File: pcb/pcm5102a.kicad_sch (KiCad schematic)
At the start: 11 parts, among them J11 PCM5102A Breakout, J12 Conn_01x03_Pin

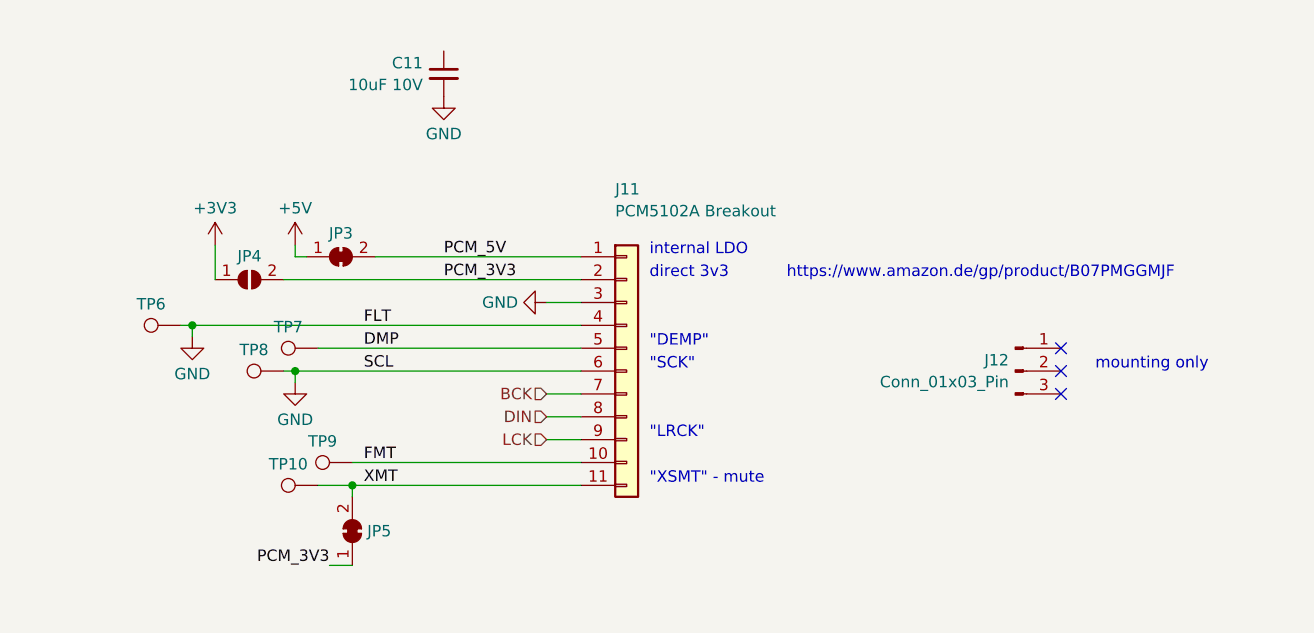
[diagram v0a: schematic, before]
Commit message: work on PCB: line out + power done ; removed amplifier from board
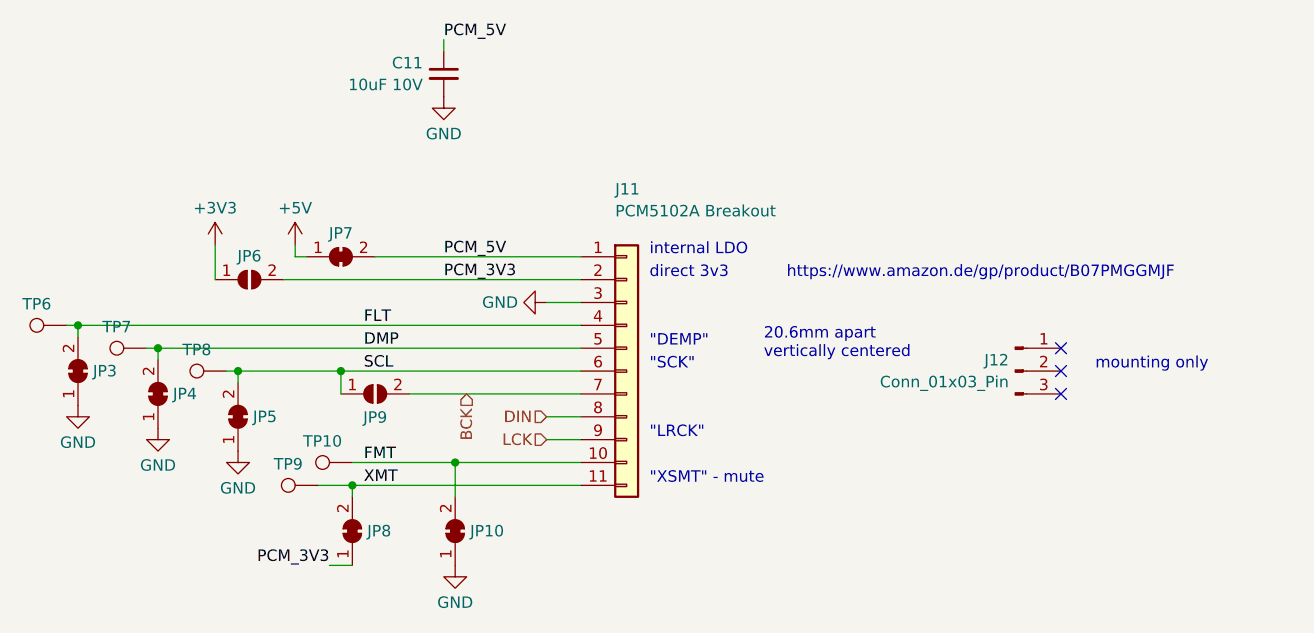
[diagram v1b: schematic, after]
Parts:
- added JP10, JP3, JP4, JP5: SolderJumper_2_Bridged, Jumper:SolderJumper-2_P1.3mm_Bridged_Pad1.0x1.5mm, symbol Jumper:SolderJumper_2_Bridged
- added JP9: SolderJumper_2_Open, Jumper:SolderJumper-2_P1.3mm_Open_Pad1.0x1.5mm, symbol Jumper:SolderJumper_2_Open
- renumbered JP4 to JP6, JP3 to JP7, JP5 to JP8, TP9 to TP10, TP10 to TP9
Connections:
- net BCK: now also JP9.2 (B)
- net DMP: now also JP4.2 (B)
- net FMT: now also JP10.2 (B)
- net GND: now also JP10.1 (A), JP3.1 (A), JP4.1 (A), JP5.1 (A); no longer J11.4 (Pin_4), J11.6 (Pin_6), TP6.1, TP8.1
- net PCM_5V: now also C11.1
- new net FLT: J11.4 (Pin_4), JP3.2 (B), TP6.1
- new net SCL: J11.6 (Pin_6), JP5.2 (B), JP9.1 (A), TP8.1
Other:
- note added: "20.6mm apart vertically centered"
- moved on the sheet: TP6, TP7, TP8

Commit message: PCB done
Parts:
- J11: footprint Connector_PinHeader_2.54mm:PinHeader_1x11_P2.54mm_Vertical -> Connector_PinSocket_2.54mm:PinSocket_1x11_P2.54mm_Vertical
- J12: footprint Connector_PinHeader_2.54mm:PinHeader_1x03_P2.54mm_Vertical -> Connector_PinSocket_2.54mm:PinSocket_1x03_P2.54mm_Vertical
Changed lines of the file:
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@@
-    (effects (font (size 1.27 1.27)) (justify left bottom))
-  )
-  (label "XMT" (at 101.6 105.41 0) (fields_autoplaced)
     (effects (font (size 1.27 1.27)) (justify left bottom))
   )
@@
   )
   (hierarchical_label "BCK" (shape input) (at 113.03 95.25 270) (fields_autoplaced)
+    (effects (font (size 1.27 1.27)) (justify right))
+  )
+  (hierarchical_label "XMT" (shape input) (at 97.79 105.41 270) (fields_autoplaced)
     (effects (font (size 1.27 1.27)) (justify right))
   )
@@
       (effects (font (size 1.27 1.27)) (justify left))
     )
-    (property "Footprint" "Connector_PinHeader_2.54mm:PinHeader_1x11_P2.54mm_Vertical" (at 130.81 92.71 0)
+    (property "Footprint" "Connector_PinSocket_2.54mm:PinSocket_1x11_P2.54mm_Vertical" (at 130.81 92.71 0)
       (effects (font (size 1.27 1.27)) hide)
     )
@@
       (effects (font (size 1.27 1.27)) (justify right))
     )
-    (property "Footprint" "Connector_PinHeader_2.54mm:PinHeader_1x03_P2.54mm_Vertical" (at 173.99 92.71 0)
-      (effects (font (size 1.27 1.27)) hide)
-    )
+    (property "Footprint" "Connector_PinSocket_2.54mm:PinSocket_1x03_P2.54mm_Vertical" (at 173.99 92.71 0)
+      (effects (font (size 1.27 1.27)) hide)
+    )

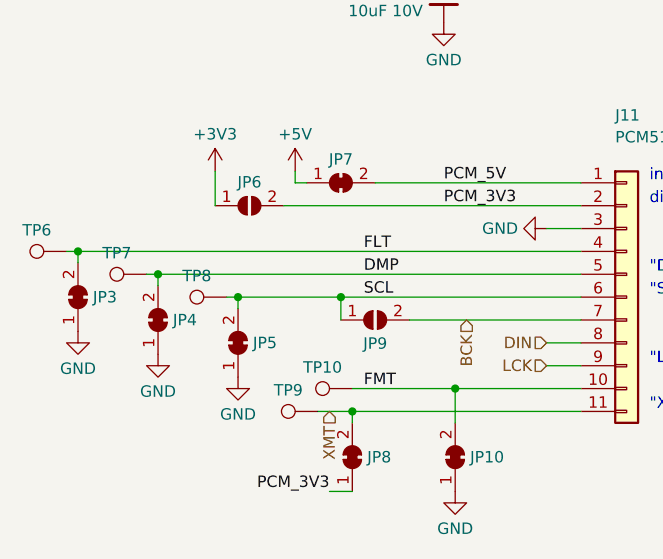
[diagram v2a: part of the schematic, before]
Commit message: moved to Kicad 8
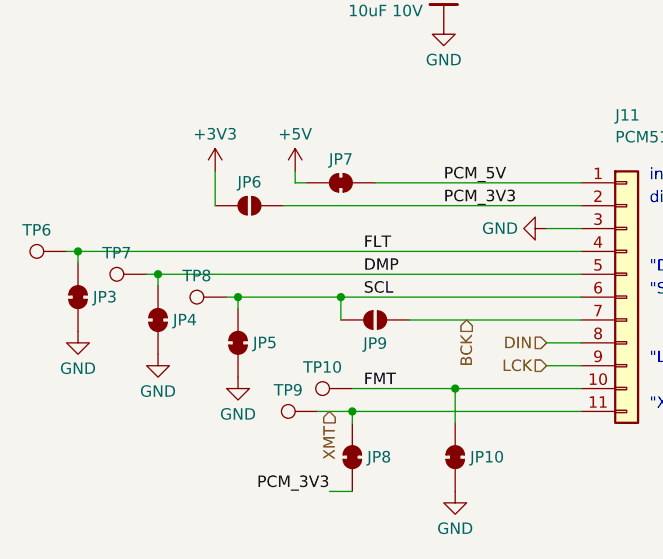
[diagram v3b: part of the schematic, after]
